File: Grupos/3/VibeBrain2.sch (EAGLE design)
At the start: 37 parts, among them J1 TC2030-IDC, U1 TPS62203DBVR, U2 DRV2605LDGSR, U3 MCP73831T-2ACI/OT

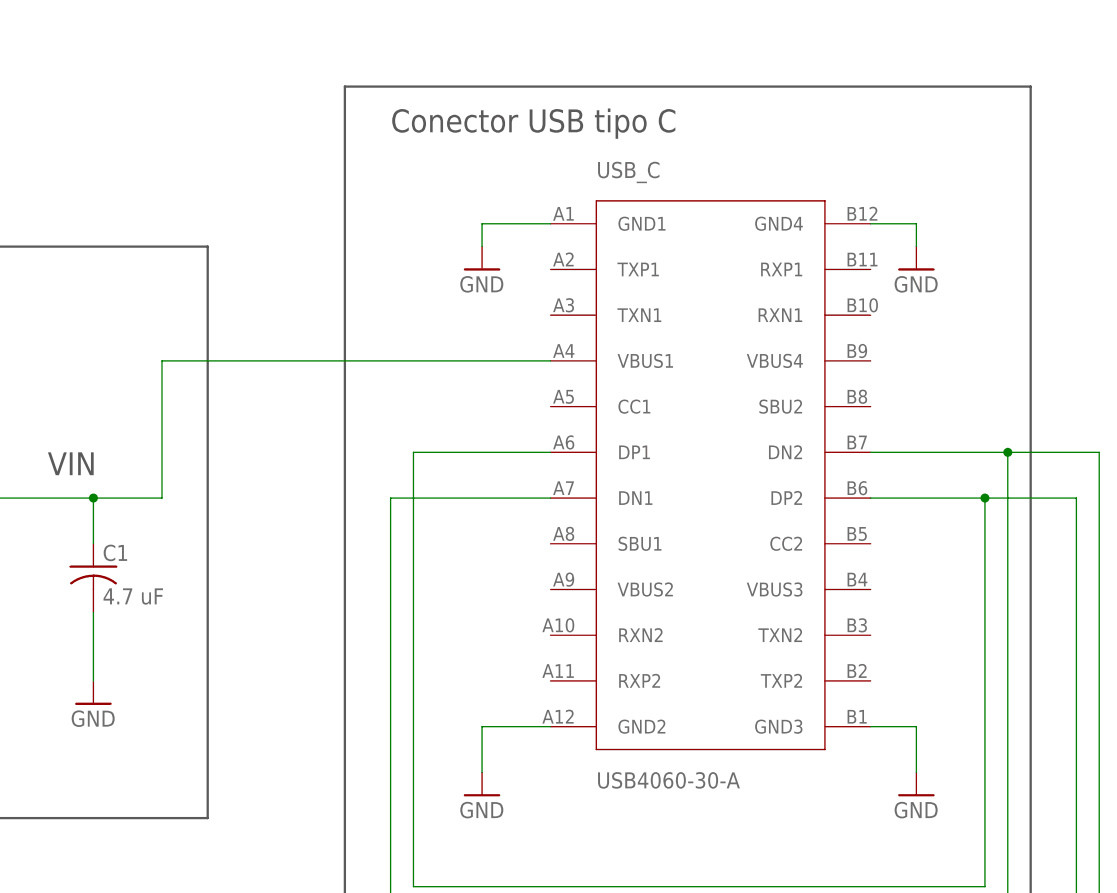
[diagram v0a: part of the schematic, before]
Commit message: Se agregan resistencias de CC, sin embargo una debe ser cableada manualmente
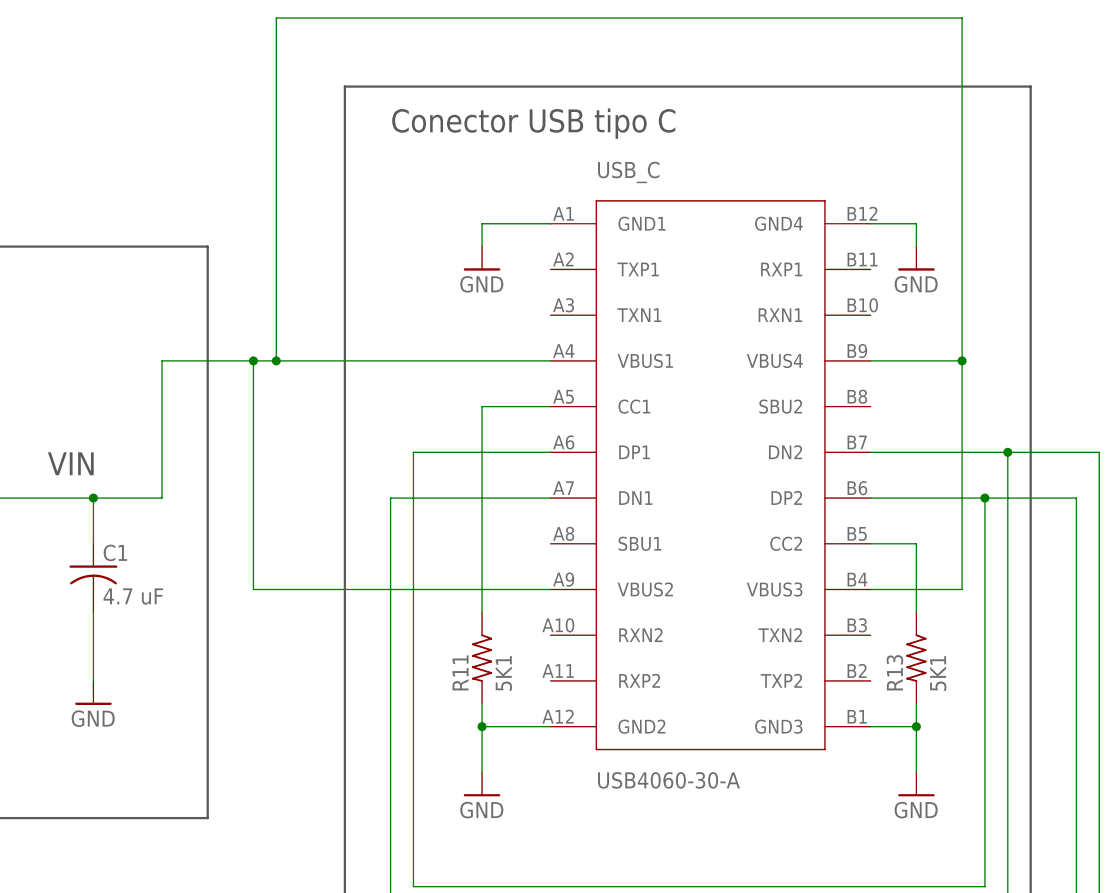
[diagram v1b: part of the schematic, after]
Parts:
- added R11, R13: 5K1, rcl:R-US_R0402
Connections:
- new net N$25: R11.1, USB_C.CC1
- new net N$26: R13.1, USB_C.CC2
- net GND: now also R11.2, R13.2
- net VDD: now also USB_C.VBUS2, USB_C.VBUS3, USB_C.VBUS4
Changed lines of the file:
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@@
 <drawing>
 <settings>
-<setting alwaysvectorfont="no"/>
+<setting alwaysvectorfont="yes"/>
 <setting verticaltext="up"/>
 </settings>
@@
 <attribute name="PARTNO" value="LQW15DN100M00D"/>
 </part>
+<part name="R11" library="rcl" library_urn="urn:adsk.eagle:library:334" deviceset="R-US_" device="R0402" package3d_urn="urn:adsk.eagle:package:23547/3" value="5K1">
+<spice>
+<pinmapping spiceprefix="R">
+<pinmap gate="G$1" pin="1" pinorder="1"/>
+<pinmap gate="G$1" pin="2" pinorder="2"/>
+</pinmapping>
+</spice>
+<attribute name="PARTNO" value="RC0402FR-075K1L"/>
+</part>
+<part name="R13" library="rcl" library_urn="urn:adsk.eagle:library:334" deviceset="R-US_" device="R0402" package3d_urn="urn:adsk.eagle:package:23547/3" value="5K1">
+<spice>
+<pinmapping spiceprefix="R">
+<pinmap gate="G$1" pin="1" pinorder="1"/>
+<pinmap gate="G$1" pin="2" pinorder="2"/>
+</pinmapping>
+</spice>
+<attribute name="PARTNO" value="RC0402FR-075K1L"/>
+</part>
 </parts>
 <sheets>
@@
 <attribute name="PARTNO" x="-30.48" y="68.58" size="1.778" layer="96" display="off"/>
 </instance>
+<instance part="R11" gate="G$1" x="261.62" y="40.64" smashed="yes" rot="R270">
+<attribute name="NAME" x="260.1214" y="36.83" size="1.778" layer="95" rot="R90"/>
+<attribute name="VALUE" x="264.922" y="36.83" size="1.778" layer="96" rot="R90"/>
+<attribute name="PARTNO" x="261.62" y="40.64" size="1.778" layer="96" rot="R270" display="off"/>
+</instance>
+<instance part="R13" gate="G$1" x="309.88" y="40.64" smashed="yes" rot="R270">
+<attribute name="NAME" x="308.3814" y="36.83" size="1.778" layer="95" rot="R90"/>
+<attribute name="VALUE" x="313.182" y="36.83" size="1.778" layer="96" rot="R90"/>
+<attribute name="PARTNO" x="309.88" y="40.64" size="1.778" layer="96" rot="R270" display="off"/>
+</instance>
 </instances>
 <busses>
@@
 <wire x1="261.62" y1="33.02" x2="261.62" y2="27.94" width="0.1524" layer="91"/>
 <pinref part="USB_C" gate="G$1" pin="GND2"/>
+<pinref part="R11" gate="G$1" pin="2"/>
+<wire x1="261.62" y1="33.02" x2="261.62" y2="35.56" width="0.1524" layer="91"/>
+<junction x="261.62" y="33.02"/>
 </segment>
 <segment>
@@
 <wire x1="309.88" y1="33.02" x2="309.88" y2="27.94" width="0.1524" layer="91"/>
 <pinref part="USB_C" gate="G$1" pin="GND3"/>
+<pinref part="R13" gate="G$1" pin="2"/>
+<wire x1="309.88" y1="35.56" x2="309.88" y2="33.02" width="0.1524" layer="91"/>
+<junction x="309.88" y="33.02"/>
 </segment>
 <segment>
@@
 <junction x="218.44" y="58.42"/>
 <pinref part="U3" gate="G$1" pin="VDD"/>
-<wire x1="269.24" y1="73.66" x2="226.06" y2="73.66" width="0.1524" layer="91"/>
+<wire x1="269.24" y1="73.66" x2="238.76" y2="73.66" width="0.1524" layer="91"/>
+<wire x1="238.76" y1="73.66" x2="236.22" y2="73.66" width="0.1524" layer="91"/>
+<wire x1="236.22" y1="73.66" x2="226.06" y2="73.66" width="0.1524" layer="91"/>
 <wire x1="226.06" y1="73.66" x2="226.06" y2="58.42" width="0.1524" layer="91"/>
 <wire x1="226.06" y1="58.42" x2="218.44" y2="58.42" width="0.1524" layer="91"/>
 <pinref part="USB_C" gate="G$1" pin="VBUS1"/>
 <pinref part="C1" gate="G$1" pin="1"/>
+<pinref part="USB_C" gate="G$1" pin="VBUS2"/>
+<wire x1="269.24" y1="48.26" x2="236.22" y2="48.26" width="0.1524" layer="91"/>
+<wire x1="236.22" y1="48.26" x2="236.22" y2="73.66" width="0.1524" layer="91"/>
+<junction x="236.22" y="73.66"/>
+<pinref part="USB_C" gate="G$1" pin="VBUS4"/>
+<wire x1="304.8" y1="73.66" x2="314.96" y2="73.66" width="0.1524" layer="91"/>
+<wire x1="314.96" y1="73.66" x2="314.96" y2="111.76" width="0.1524" layer="91"/>
+<wire x1="314.96" y1="111.76" x2="238.76" y2="111.76" width="0.1524" layer="91"/>
+<wire x1="238.76" y1="111.76" x2="238.76" y2="73.66" width="0.1524" layer="91"/>
+<junction x="238.76" y="73.66"/>
+<pinref part="USB_C" gate="G$1" pin="VBUS3"/>
+<wire x1="304.8" y1="48.26" x2="314.96" y2="48.26" width="0.1524" layer="91"/>
+<wire x1="314.96" y1="48.26" x2="314.96" y2="73.66" width="0.1524" layer="91"/>
+<junction x="314.96" y="73.66"/>
 </segment>
 </net>
@@
 </segment>
 </net>
+<net name="N$25" class="0">
+<segment>
+<pinref part="R11" gate="G$1" pin="1"/>
+<pinref part="USB_C" gate="G$1" pin="CC1"/>
+<wire x1="261.62" y1="45.72" x2="261.62" y2="68.58" width="0.1524" layer="91"/>
+<wire x1="261.62" y1="68.58" x2="269.24" y2="68.58" width="0.1524" layer="91"/>
+</segment>
+</net>
+<net name="N$26" class="0">
+<segment>
+<pinref part="USB_C" gate="G$1" pin="CC2"/>
+<pinref part="R13" gate="G$1" pin="1"/>
+<wire x1="304.8" y1="53.34" x2="309.88" y2="53.34" width="0.1524" layer="91"/>
+<wire x1="309.88" y1="53.34" x2="309.88" y2="45.72" width="0.1524" layer="91"/>
+</segment>
+</net>
